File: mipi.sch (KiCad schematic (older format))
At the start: 4 parts, among them Q1101 2SK3018, Q1102 2SK3018

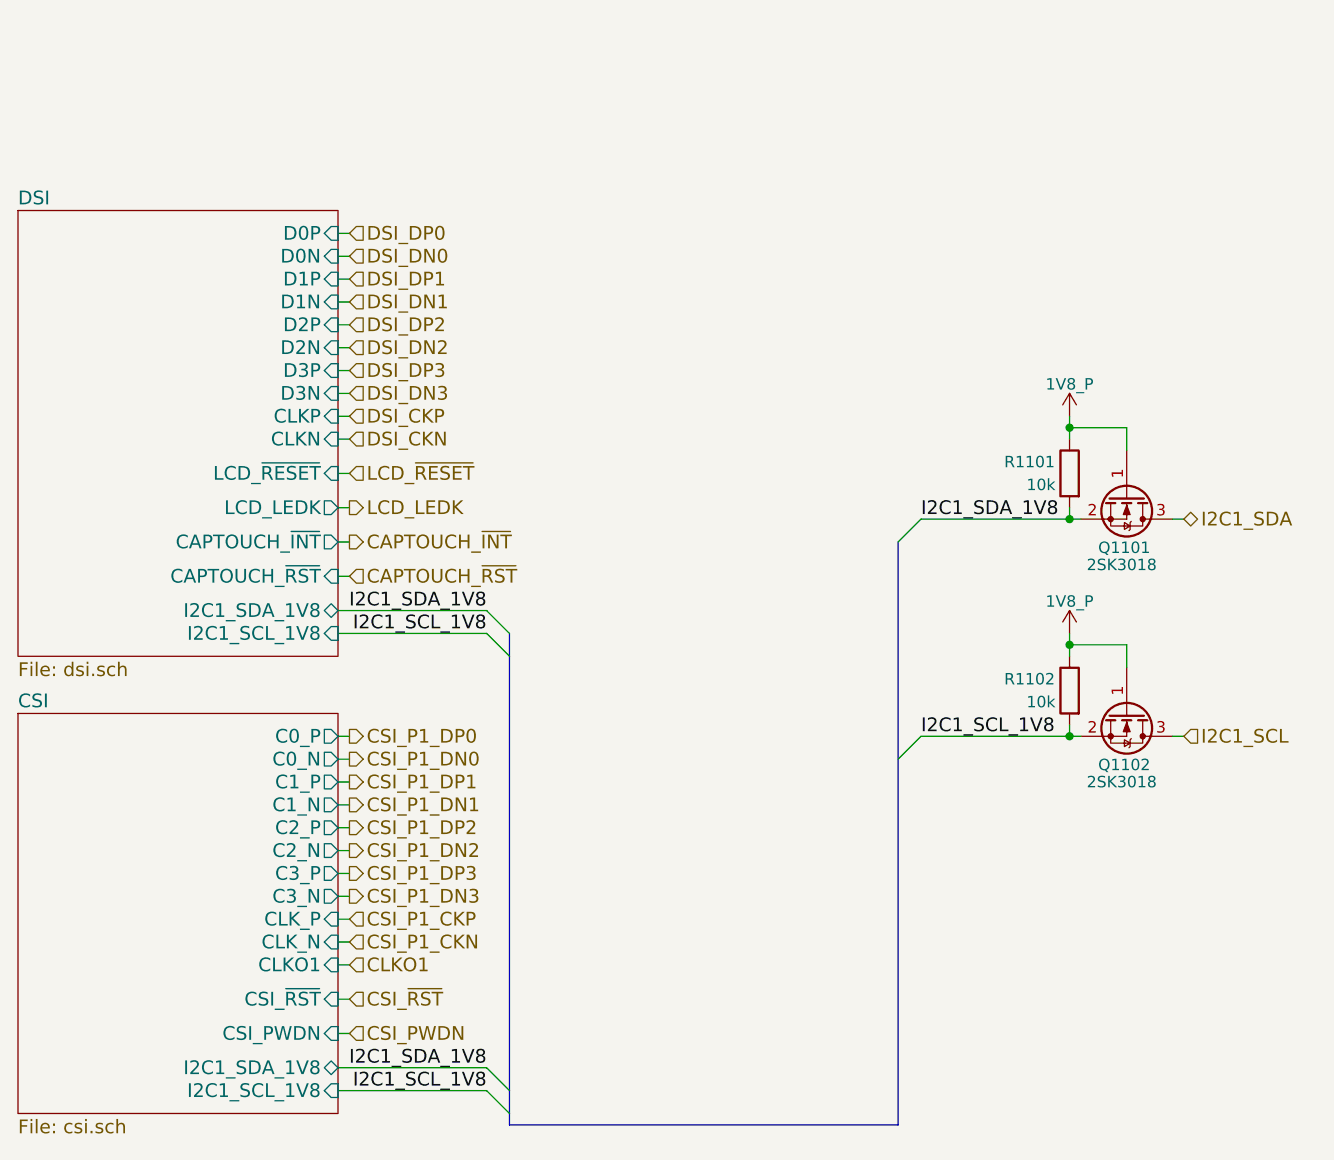
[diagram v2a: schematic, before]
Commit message: Move more symbols, sheets, and pins around on the front sheet to make it even clearer, bring back the old hierarchical structure (again), bring back each sheet's title, add large text "titles" to each sheet reflecting what they are for
Still need to double check everything on the first page.
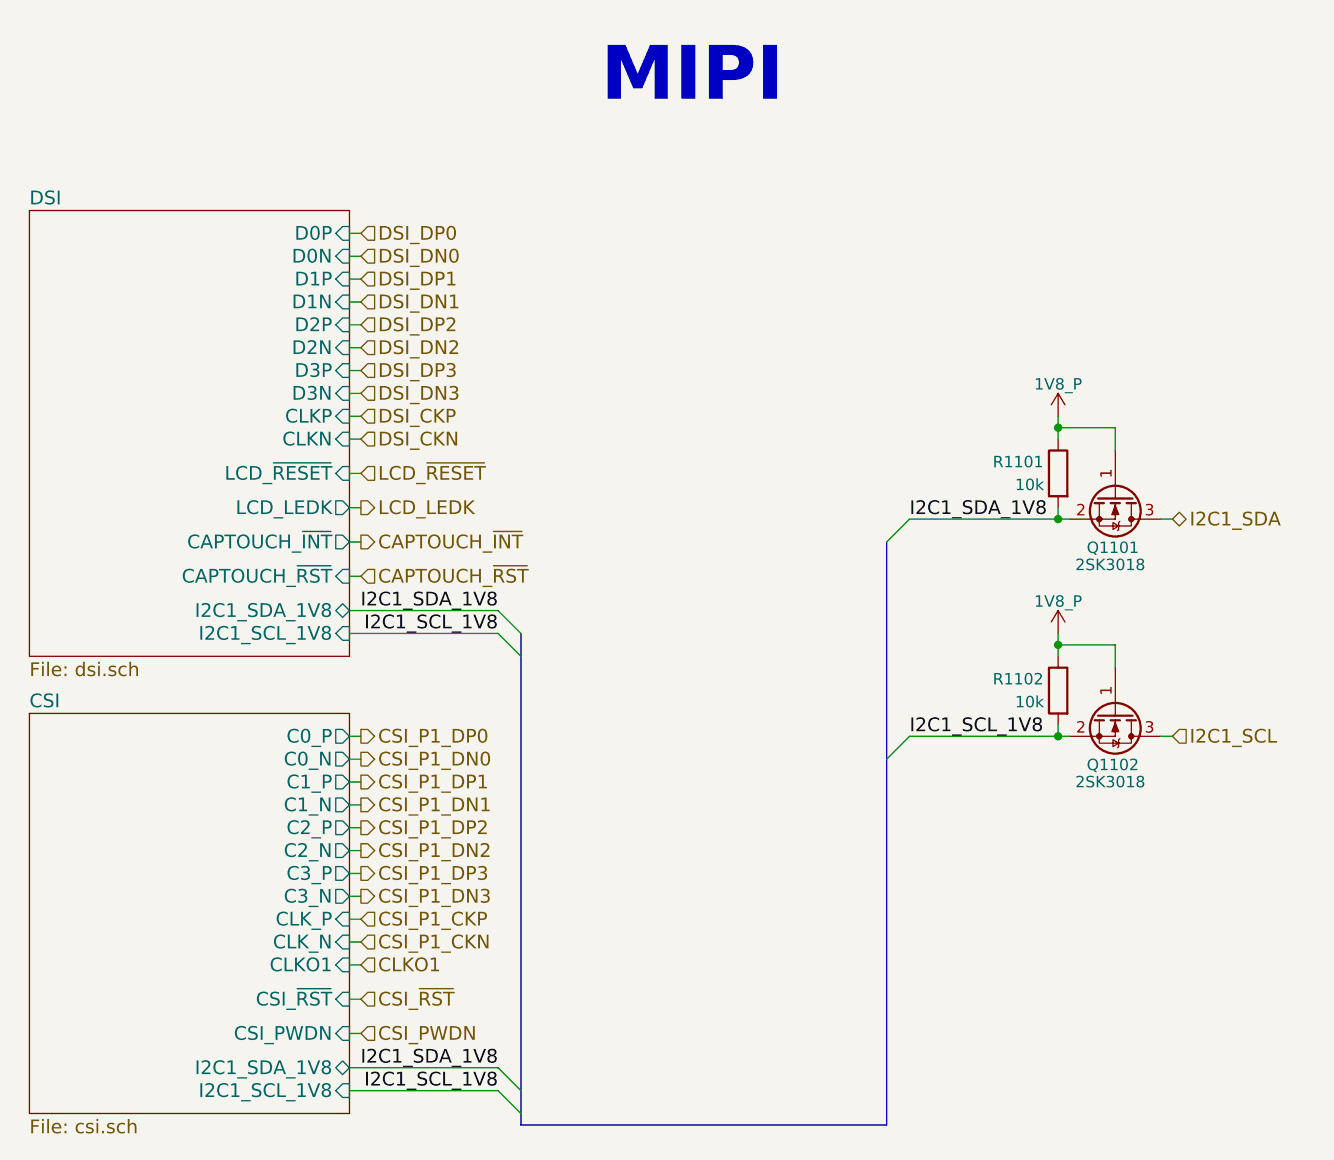
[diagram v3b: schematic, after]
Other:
- note added: "MIPI"
- moved on the sheet: Q1101, Q1102, R1101, R1102

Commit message: Make all differential pair signal names end in P/N so that diff routing works when in layout
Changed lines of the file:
@@
 	4500 2050 4550 2050
 Text HLabel 4550 2050 2    60   Input ~ 0
-DSI_DP0
+DSI_D0P
 Text HLabel 4550 2250 2    60   Input ~ 0
-DSI_DP1
+DSI_D1P
 Text HLabel 4550 2450 2    60   Input ~ 0
-DSI_DP2
+DSI_D2P
 Text HLabel 4550 2650 2    60   Input ~ 0
-DSI_DP3
+DSI_D3P
 Text HLabel 4550 2150 2    60   Input ~ 0
-DSI_DN0
+DSI_D0N
 Text HLabel 4550 2350 2    60   Input ~ 0
-DSI_DN1
+DSI_D1N
 Text HLabel 4550 2550 2    60   Input ~ 0
-DSI_DN2
+DSI_D2N
 Text HLabel 4550 2750 2    60   Input ~ 0
-DSI_DN3
+DSI_D3N
 Text HLabel 4550 4250 2    60   Output ~ 0
-CSI_P1_DP0
+CSI_P1_D0P
 Text HLabel 4550 4450 2    60   Output ~ 0
-CSI_P1_DP1
+CSI_P1_D1P
 Text HLabel 4550 4650 2    60   Output ~ 0
-CSI_P1_DP2
+CSI_P1_D2P
 Text HLabel 4550 4850 2    60   Output ~ 0
-CSI_P1_DP3
+CSI_P1_D3P
 Text HLabel 4550 4350 2    60   Output ~ 0
-CSI_P1_DN0
+CSI_P1_D0N
 Text HLabel 4550 4550 2    60   Output ~ 0
-CSI_P1_DN1
+CSI_P1_D1N
 Text HLabel 4550 4750 2    60   Output ~ 0
-CSI_P1_DN2
+CSI_P1_D2N
 Text HLabel 4550 4950 2    60   Output ~ 0
-CSI_P1_DN3
+CSI_P1_D3N
 Text HLabel 4550 2850 2    60   Input ~ 0
 DSI_CKP

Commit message: Replace 2SK3018 NFET with FDV301N
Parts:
- Q1101, Q1102: value 2SK3018 -> FDV301N; footprint dvk-mx8m-bsb:2SK3018 -> TO_SOT_Packages_SMD:SOT-23; Distrib Link https://www.mouser.com/ProductDetail/Micro-Commercial-Compo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 -> https://www.tme.eu/en/details/fdv301n/smd-n-channel-transis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; Distrib PN 833-2SK3018-TP -> FDV301N; MFG Name Micro Commercial Co -> ON Semiconductor; MFG Part Num 2SK3018-TP -> FDV301N; Others https://www.digikey.com/product-detail/en/micro-commercial-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 -> https://www.arrow.com/en/products/fdv301n/on-semiconductor
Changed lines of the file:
@@
 I2C1_SCL
 $Comp
-L 1V8_P #PWR0178
+L 1V8_P #PWR1101
 U 1 1 5B1803EF
 P 7600 2850
-F 0 "#PWR0178" H 7600 2700 50  0001 C CNN
+F 0 "#PWR1101" H 7600 2700 50  0001 C CNN
 F 1 "1V8_P" H 7600 2990 50  0000 C CNN
 F 2 "" H 7600 2850 50  0001 C CNN
@@
 $EndComp
 $Comp
-L 1V8_P #PWR0179
+L 1V8_P #PWR1102
 U 1 1 5B180400
 P 7600 3800
-F 0 "#PWR0179" H 7600 3650 50  0001 C CNN
+F 0 "#PWR1102" H 7600 3650 50  0001 C CNN
 F 1 "1V8_P" H 7600 3940 50  0000 C CNN
 F 2 "" H 7600 3800 50  0001 C CNN
@@
 Wire Wire Line
 	4500 3550 4550 3550
-$Comp
-L Q_NMOS_GSD Q1102
-U 1 1 5B58BACE
-P 7850 4150
-F 0 "Q1102" V 8075 4025 50  0000 L CNN
-F 1 "2SK3018" V 8150 3975 50  0000 L CNN
-F 2 "dvk-mx8m-bsb:2SK3018" H 8050 4250 50  0001 C CNN
-F 3 "http://www.mccsemi.com/up_pdf/2SK3018(SOT-323).pdf" H 7850 4150 50  0001 C CNN
-F 4 "Micro Commercial Co" V 7850 4150 60  0001 C CNN "MFG Name"
-F 5 "2SK3018-TP" V 7850 4150 60  0001 C CNN "MFG Part Num"
-F 6 "833-2SK3018-TP" V 7850 4150 60  0001 C CNN "Distrib PN"
-F 7 "https://www.mouser.com/ProductDetail/Micro-Commercial-Components-MCC/2SK3018-TP?qs=sGAEpiMZZMtI26rxh1qzjnDHXOVLFYvgyLpQIEHdJp0%3d" V 7850 4150 60  0001 C CNN "Distrib Link"
-F 8 "-" V 7850 4150 60  0001 C CNN "Tolerance"
-F 9 "https://www.digikey.com/product-detail/en/micro-commercial-co/2SK3018-TP/2SK3018-TPMSCT-ND/6616131" V 7850 4150 60  0001 C CNN "Others"
-	1    7850 4150
-	0    1    1    0
-$EndComp
-$Comp
-L Q_NMOS_GSD Q1101
-U 1 1 5B58FE44
-P 7850 3200
-F 0 "Q1101" V 8075 3075 50  0000 L CNN
-F 1 "2SK3018" V 8150 3025 50  0000 L CNN
-F 2 "dvk-mx8m-bsb:2SK3018" H 8050 3300 50  0001 C CNN
-F 3 "http://www.mccsemi.com/up_pdf/2SK3018(SOT-323).pdf" H 7850 3200 50  0001 C CNN
-F 4 "Micro Commercial Co" V 7850 3200 60  0001 C CNN "MFG Name"
-F 5 "2SK3018-TP" V 7850 3200 60  0001 C CNN "MFG Part Num"
-F 6 "833-2SK3018-TP" V 7850 3200 60  0001 C CNN "Distrib PN"
-F 7 "https://www.mouser.com/ProductDetail/Micro-Commercial-Components-MCC/2SK3018-TP?qs=sGAEpiMZZMtI26rxh1qzjnDHXOVLFYvgyLpQIEHdJp0%3d" V 7850 3200 60  0001 C CNN "Distrib Link"
-F 8 "-" V 7850 3200 60  0001 C CNN "Tolerance"
-F 9 "https://www.digikey.com/product-detail/en/micro-commercial-co/2SK3018-TP/2SK3018-TPMSCT-ND/6616131" V 7850 3200 60  0001 C CNN "Others"
-	1    7850 3200
-	0    1    1    0
-$EndComp
 Wire Wire Line
 	4500 5250 4550 5250
@@
 	5250 3800 5250 5950
 Wire Bus Line
-	5250 5950 6850 5950
+	6850 5950 5250 5950
 Wire Bus Line
-	6850 5950 6850 3400
+	6850 3400 6850 5950
 Entry Wire Line
 	6950 3300 6850 3400
@@
 Text Notes 5600 1500 0    236  ~ 47
 MIPI
+$Comp
+L Q_NMOS_GSD Q1102
+U 1 1 5B2D5EAE
+P 7850 4150
+F 0 "Q1102" V 8075 4025 50  0000 L CNN
+F 1 "FDV301N" V 8150 3975 50  0000 L CNN
+F 2 "TO_SOT_Packages_SMD:SOT-23" H 8050 4250 50  0001 C CNN
+F 3 "http://www.onsemi.com/pub/Collateral/FDV301N-D.PDF" H 7850 4150 50  0001 C CNN
+F 4 "ON Semiconductor" V 7850 4150 60  0001 C CNN "MFG Name"
+F 5 "FDV301N" V 7850 4150 60  0001 C CNN "MFG Part Num"
+F 6 "FDV301N" V 7850 4150 60  0001 C CNN "Distrib PN"
+F 7 "https://www.tme.eu/en/details/fdv301n/smd-n-channel-transistors/on-semiconductor-fairchild/" V 7850 4150 60  0001 C CNN "Distrib Link"
+F 8 "-" V 7850 4150 60  0001 C CNN "Tolerance"
+F 9 "https://www.arrow.com/en/products/fdv301n/on-semiconductor" V 7850 4150 60  0001 C CNN "Others"
+	1    7850 4150
+	0    1    1    0
+$EndComp
+$Comp
+L Q_NMOS_GSD Q1101
+U 1 1 5B2D7A3D
+P 7850 3200
+F 0 "Q1101" V 8075 3075 50  0000 L CNN
+F 1 "FDV301N" V 8150 3025 50  0000 L CNN
+F 2 "TO_SOT_Packages_SMD:SOT-23" H 8050 3300 50  0001 C CNN
+F 3 "http://www.onsemi.com/pub/Collateral/FDV301N-D.PDF" H 7850 3200 50  0001 C CNN
+F 4 "ON Semiconductor" V 7850 3200 60  0001 C CNN "MFG Name"
+F 5 "FDV301N" V 7850 3200 60  0001 C CNN "MFG Part Num"
+F 6 "FDV301N" V 7850 3200 60  0001 C CNN "Distrib PN"
+F 7 "https://www.tme.eu/en/details/fdv301n/smd-n-channel-transistors/on-semiconductor-fairchild/" V 7850 3200 60  0001 C CNN "Distrib Link"
+F 8 "-" V 7850 3200 60  0001 C CNN "Tolerance"
+F 9 "https://www.arrow.com/en/products/fdv301n/on-semiconductor" V 7850 3200 60  0001 C CNN "Others"
+	1    7850 3200
+	0    1    1    0
+$EndComp
 $EndSCHEMATC
